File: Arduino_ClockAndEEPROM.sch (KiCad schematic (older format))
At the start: 13 parts, among them U1 24LC1025, U2 24LC1025, U3 DS1337_8pin_Bayterek, U4 ATmega328P-AU, Y1 Crystal, Y2 Crystal

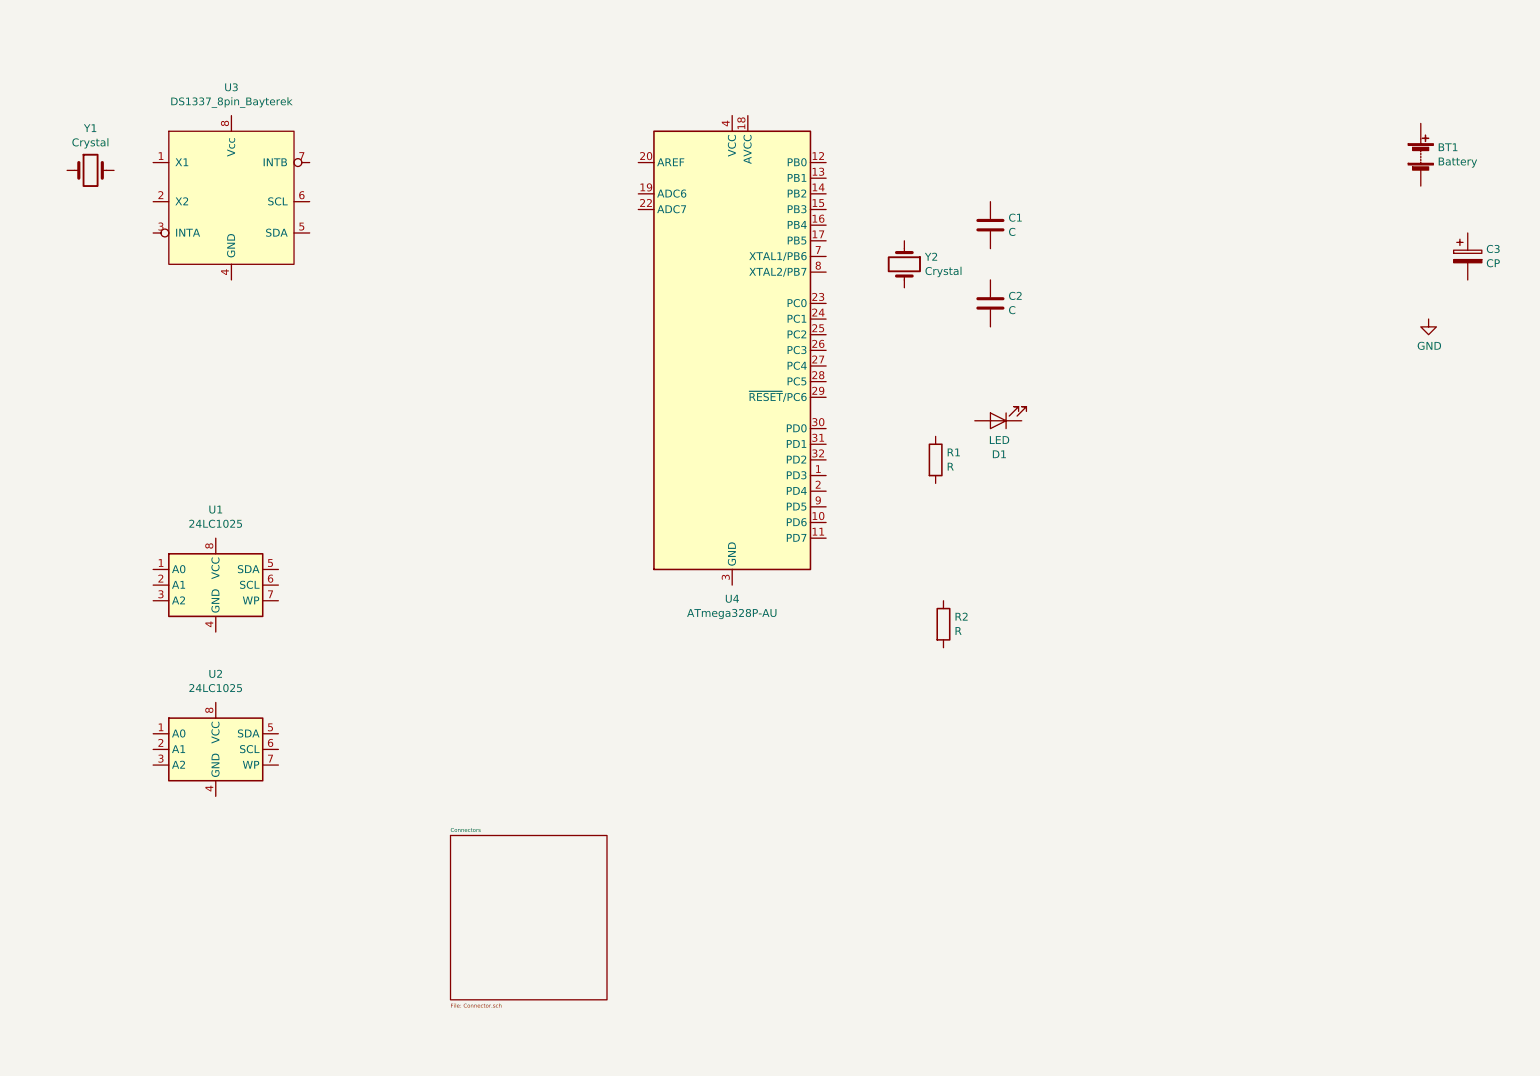
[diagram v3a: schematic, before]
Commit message: Completed associations and added component values.
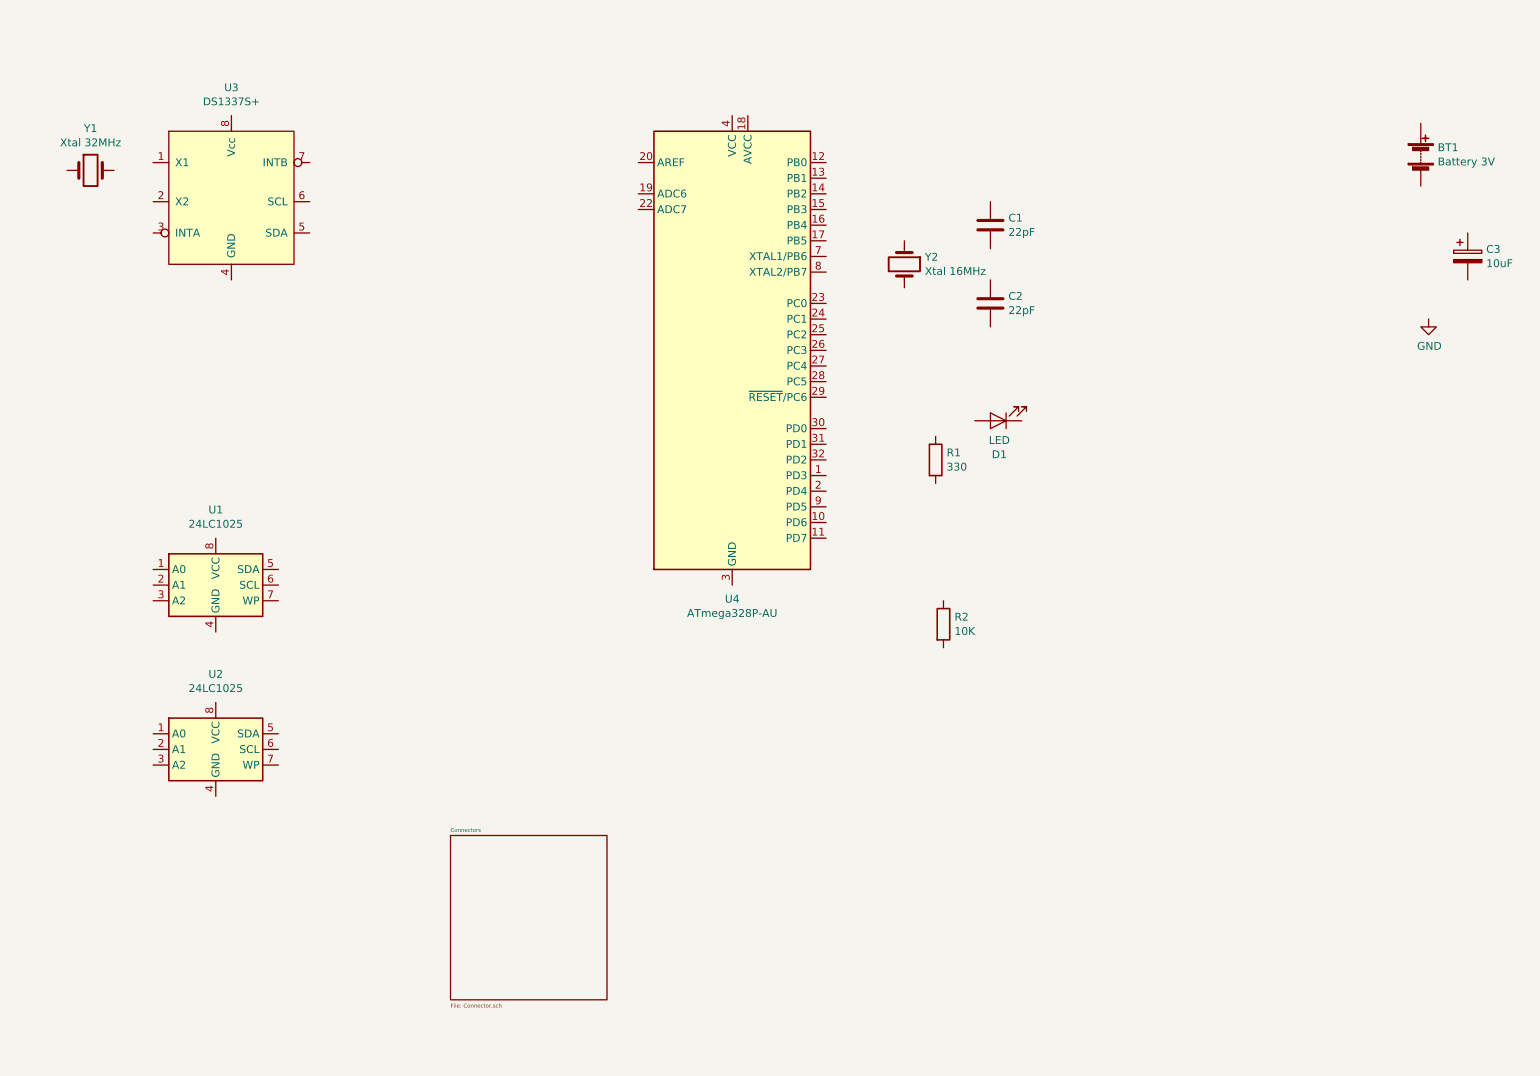
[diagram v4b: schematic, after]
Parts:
- BT1: value Battery -> Battery 3V; footprint (none) -> Connector_PinHeader_2.54mm:PinHeader_1x02_P2.54mm_Vertical
- C1, C2: value C -> 22pF; footprint (none) -> Capacitor_SMD:C_0805_2012Metric_Pad1.15x1.40mm_HandSolder
- C3: value CP -> 10uF; footprint (none) -> Capacitor_SMD:C_0805_2012Metric_Pad1.15x1.40mm_HandSolder
- D1: footprint (none) -> LED_SMD:LED_0805_2012Metric_Pad1.15x1.40mm_HandSolder
- R1: value R -> 330; footprint (none) -> Resistor_SMD:R_0815_2038Metric_Pad1.53x4.00mm_HandSolder
- R2: value R -> 10K; footprint (none) -> Resistor_SMD:R_0815_2038Metric_Pad1.53x4.00mm_HandSolder
- U1, U2: footprint (none) -> Package_SO:SOIJ-8_5.3x5.3mm_P1.27mm
- U3: value DS1337_8pin_Bayterek -> DS1337S+; footprint (none) -> Package_SO:SO-8_5.3x6.2mm_P1.27mm
- Y1: value Crystal -> Xtal 32MHz; footprint (none) -> Crystal:Crystal_SMD_MicroCrystal_CC7V-T1A-2Pin_3.2x1.5mm
- Y2: value Crystal -> Xtal 16MHz; footprint (none) -> Crystal:Crystal_SMD_5032-2Pin_5.0x3.2mm_HandSoldering
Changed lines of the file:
@@
 P 9750 1750
 F 0 "BT1" H 9858 1796 50  0000 L CNN
-F 1 "Battery" H 9858 1705 50  0000 L CNN
-F 2 "" V 9750 1810 50  0001 C CNN
+F 1 "Battery 3V" H 9858 1705 50  0000 L CNN
+F 2 "Connector_PinHeader_2.54mm:PinHeader_1x02_P2.54mm_Vertical" V 9750 1810 50  0001 C CNN
 F 3 "~" V 9750 1810 50  0001 C CNN
 	1    9750 1750
@@
 P 7000 2200
 F 0 "C1" H 7115 2246 50  0000 L CNN
-F 1 "C" H 7115 2155 50  0000 L CNN
-F 2 "" H 7038 2050 50  0001 C CNN
+F 1 "22pF" H 7115 2155 50  0000 L CNN
+F 2 "Capacitor_SMD:C_0805_2012Metric_Pad1.15x1.40mm_HandSolder" H 7038 2050 50  0001 C CNN
 F 3 "~" H 7000 2200 50  0001 C CNN
 	1    7000 2200
@@
 P 7000 2700
 F 0 "C2" H 7115 2746 50  0000 L CNN
-F 1 "C" H 7115 2655 50  0000 L CNN
-F 2 "" H 7038 2550 50  0001 C CNN
+F 1 "22pF" H 7115 2655 50  0000 L CNN
+F 2 "Capacitor_SMD:C_0805_2012Metric_Pad1.15x1.40mm_HandSolder" H 7038 2550 50  0001 C CNN
 F 3 "~" H 7000 2700 50  0001 C CNN
 	1    7000 2700
@@
 P 10050 2400
 F 0 "C3" H 10168 2446 50  0000 L CNN
-F 1 "CP" H 10168 2355 50  0000 L CNN
-F 2 "" H 10088 2250 50  0001 C CNN
+F 1 "10uF" H 10168 2355 50  0000 L CNN
+F 2 "Capacitor_SMD:C_0805_2012Metric_Pad1.15x1.40mm_HandSolder" H 10088 2250 50  0001 C CNN
 F 3 "~" H 10050 2400 50  0001 C CNN
 	1    10050 2400
@@
 F 0 "D1" H 7043 3666 50  0000 C CNN
 F 1 "LED" H 7043 3575 50  0000 C CNN
-F 2 "" H 7050 3450 50  0001 C CNN
+F 2 "LED_SMD:LED_0805_2012Metric_Pad1.15x1.40mm_HandSolder" H 7050 3450 50  0001 C CNN
 F 3 "~" H 7050 3450 50  0001 C CNN
 	1    7050 3450
@@
 P 6650 3700
 F 0 "R1" H 6720 3746 50  0000 L CNN
-F 1 "R" H 6720 3655 50  0000 L CNN
-F 2 "" V 6580 3700 50  0001 C CNN
+F 1 "330" H 6720 3655 50  0000 L CNN
+F 2 "Resistor_SMD:R_0815_2038Metric_Pad1.53x4.00mm_HandSolder" V 6580 3700 50  0001 C CNN
 F 3 "~" H 6650 3700 50  0001 C CNN
 	1    6650 3700
@@
 P 6700 4750
 F 0 "R2" H 6770 4796 50  0000 L CNN
-F 1 "R" H 6770 4705 50  0000 L CNN
-F 2 "" V 6630 4750 50  0001 C CNN
+F 1 "10K" H 6770 4705 50  0000 L CNN
+F 2 "Resistor_SMD:R_0815_2038Metric_Pad1.53x4.00mm_HandSolder" V 6630 4750 50  0001 C CNN
 F 3 "~" H 6700 4750 50  0001 C CNN
 	1    6700 4750
@@
 F 0 "U1" H 2050 4981 50  0000 C CNN
 F 1 "24LC1025" H 2050 4890 50  0000 C CNN
-F 2 "" H 2050 4500 50  0001 C CNN
+F 2 "Package_SO:SOIJ-8_5.3x5.3mm_P1.27mm" H 2050 4500 50  0001 C CNN
 F 3 "http://ww1.microchip.com/downloads/en/DeviceDoc/21941B.pdf" H 2050 4500 50  0001 C CNN
 	1    2050 4500
@@
 P 2750 1450
 F 0 "U3" H 2150 1579 49  0000 C CNN
-F 1 "DS1337_8pin_Bayterek" H 2150 1489 49  0000 C CNN
-F 2 "" H 2800 1550 49  0001 C CNN
+F 1 "DS1337S+" H 2150 1489 49  0000 C CNN
+F 2 "Package_SO:SO-8_5.3x6.2mm_P1.27mm" H 2800 1550 49  0001 C CNN
 F 3 "http://www.farnell.com/datasheets/2000844.pdf?_ga=2.2648176.1329014715.1559527073-834126407.1559527073" H 2800 1550 49  0001 C CNN
 	1    2750 1450
@@
 P 6450 2450
 F 0 "Y2" V 6404 2581 50  0000 L CNN
-F 1 "Crystal" V 6495 2581 50  0000 L CNN
-F 2 "" H 6450 2450 50  0001 C CNN
+F 1 "Xtal 16MHz" V 6495 2581 50  0000 L CNN
+F 2 "Crystal:Crystal_SMD_5032-2Pin_5.0x3.2mm_HandSoldering" H 6450 2450 50  0001 C CNN
 F 3 "~" H 6450 2450 50  0001 C CNN
 	1    6450 2450
@@
 P 1250 1850
 F 0 "Y1" H 1250 2118 50  0000 C CNN
-F 1 "Crystal" H 1250 2027 50  0000 C CNN
-F 2 "" H 1250 1850 50  0001 C CNN
+F 1 "Xtal 32MHz" H 1250 2027 50  0000 C CNN
+F 2 "Crystal:Crystal_SMD_MicroCrystal_CC7V-T1A-2Pin_3.2x1.5mm" H 1250 1850 50  0001 C CNN
 F 3 "~" H 1250 1850 50  0001 C CNN
 	1    1250 1850
@@
 F 0 "U2" H 2050 6031 50  0000 C CNN
 F 1 "24LC1025" H 2050 5940 50  0000 C CNN
-F 2 "" H 2050 5550 50  0001 C CNN
+F 2 "Package_SO:SOIJ-8_5.3x5.3mm_P1.27mm" H 2050 5550 50  0001 C CNN
 F 3 "http://ww1.microchip.com/downloads/en/DeviceDoc/21941B.pdf" H 2050 5550 50  0001 C CNN
 	1    2050 5550

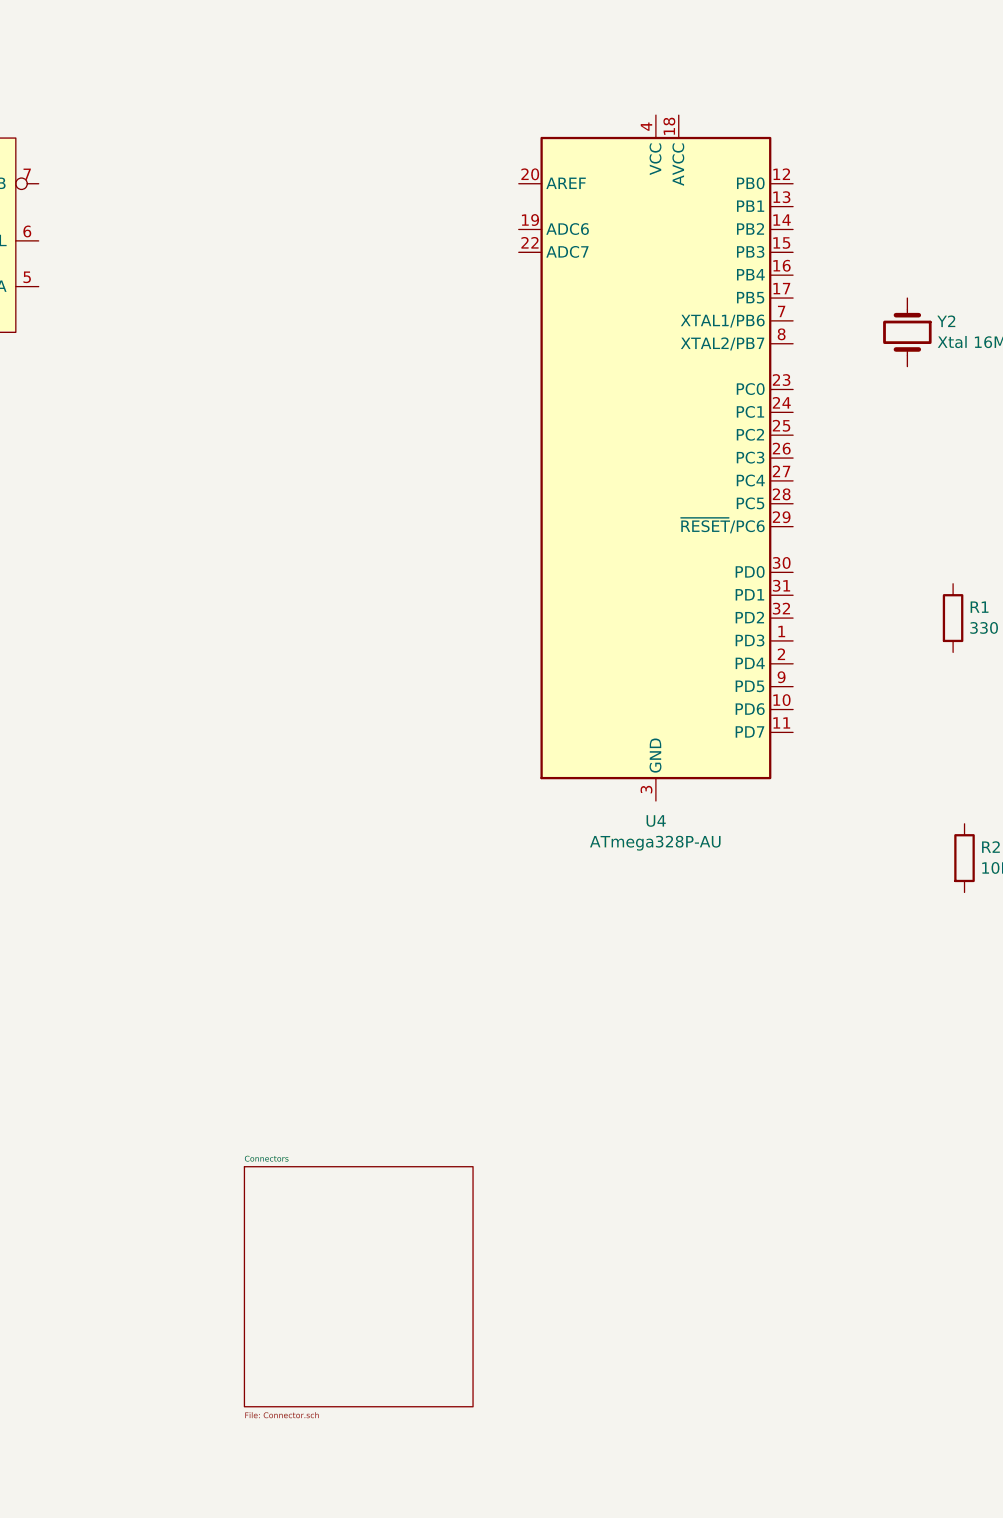
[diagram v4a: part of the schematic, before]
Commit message: Completed wiring in the connectors sheet.
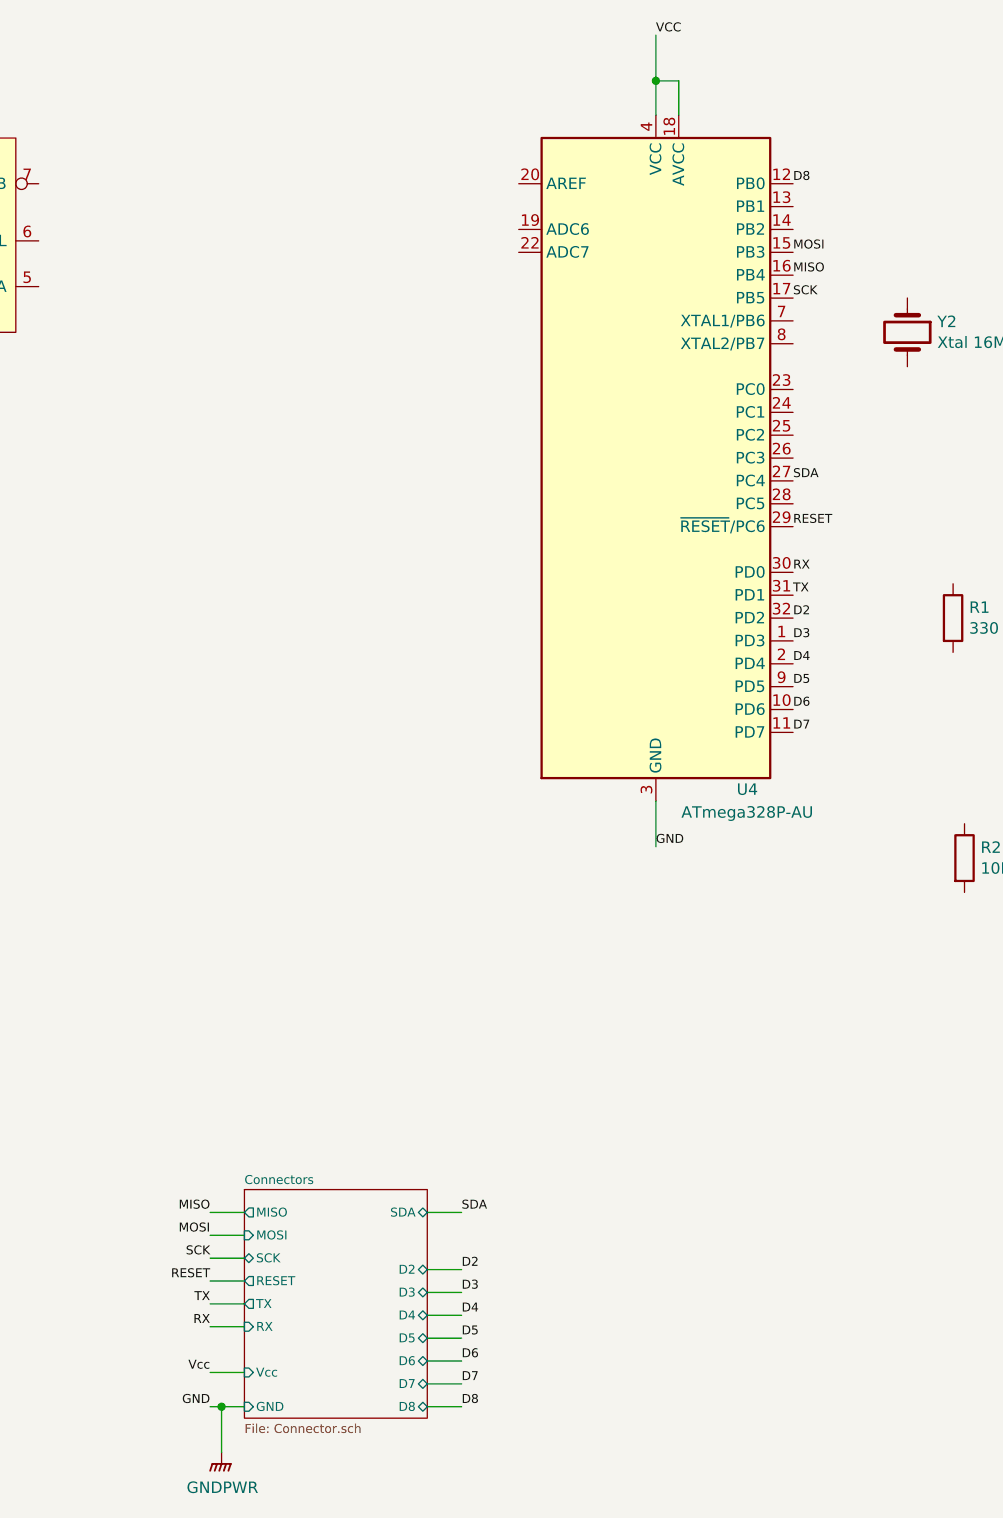
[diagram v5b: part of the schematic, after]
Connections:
- net GND: now also U4.21 (GND), U4.3 (GND), U4.5 (GND)
- net D3: now reaches U4.1 (PD3)
- net D6: now reaches U4.10 (PD6)
- net D7: now reaches U4.11 (PD7)
- net D8: now reaches U4.12 (PB0)
- net MOSI: now reaches U4.15 (PB3)
- net MISO: now reaches U4.16 (PB4)
- net SCK: now reaches U4.17 (PB5)
- net VCC: now reaches U4.18 (AVCC)
- net VCC: now also U4.4 (VCC), U4.6 (VCC)
- net D4: now reaches U4.2 (PD4)
- net SDA: now reaches U4.27 (PC4)
- net RESET: now reaches U4.29 (~RESET~/PC6)
- net RX: now reaches U4.30 (PD0)
- net TX: now reaches U4.31 (PD1)
- net D2: now reaches U4.32 (PD2)
- net D5: now reaches U4.9 (PD5)
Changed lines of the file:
@@
 U 1 1 5CF90E0E
 P 5350 3000
-F 0 "U4" H 5350 1411 50  0000 C CNN
-F 1 "ATmega328P-AU" H 5350 1320 50  0000 C CNN
+F 0 "U4" H 5750 1550 50  0000 C CNN
+F 1 "ATmega328P-AU" H 5750 1450 50  0000 C CNN
 F 2 "Package_QFP:TQFP-32_7x7mm_P0.8mm" H 5350 3000 50  0001 C CIN
 F 3 "http://ww1.microchip.com/downloads/en/DeviceDoc/ATmega328_P%20AVR%20MCU%20with%20picoPower%20Technology%20Data%20Sheet%2040001984A.pdf" H 5350 3000 50  0001 C CNN
@@
 	1    0    0    -1
 $EndComp
-$Sheet
-S 3550 6100 1000 1050
-U 5CF95995
-F0 "Connectors" 25
-F1 "Connector.sch" 25
-$EndSheet
 $Comp
 L Bayterek_Components:DS1337_8pin_Bayterek U3
@@
 	1    0    0    -1
 $EndComp
+Text Label 3400 6300 2    39   ~ 0
+MISO
+Wire Wire Line
+	3550 6300 3400 6300
+Text Label 5950 2200 0    39   ~ 0
+MISO
+Wire Wire Line
+	3550 6500 3400 6500
+Wire Wire Line
+	3550 6600 3400 6600
+Wire Wire Line
+	3550 7000 3400 7000
+Wire Wire Line
+	3550 6400 3400 6400
+Wire Wire Line
+	3550 7150 3450 7150
+Text Label 3400 6500 2    39   ~ 0
+SCK
+Text Label 3400 6600 2    39   ~ 0
+RESET
+Text Label 3400 7000 2    39   ~ 0
+Vcc
+Text Label 3400 6400 2    39   ~ 0
+MOSI
+Text Label 3400 7150 2    39   ~ 0
+GND
+Text Label 5950 2100 0    39   ~ 0
+MOSI
+Text Label 5950 2300 0    39   ~ 0
+SCK
+Text Label 5950 3300 0    39   ~ 0
+RESET
+Wire Wire Line
+	5350 1500 5350 1350
+Wire Wire Line
+	5350 1350 5450 1350
+Wire Wire Line
+	5450 1350 5450 1500
+Wire Wire Line
+	5350 1350 5350 1150
+Connection ~ 5350 1350
+Text Label 5350 1150 0    39   ~ 0
+VCC
+Wire Wire Line
+	5350 4500 5350 4700
+Text Label 5350 4700 0    39   ~ 0
+GND
+$Comp
+L power:GNDPWR #PWR?
+U 1 1 5CFC1B6B
+P 3450 7350
+F 0 "#PWR?" H 3450 7150 50  0001 C CNN
+F 1 "GNDPWR" H 3454 7196 50  0000 C CNN
+F 2 "" H 3450 7300 50  0001 C CNN
+F 3 "" H 3450 7300 50  0001 C CNN
+	1    3450 7350
+	1    0    0    -1
+$EndComp
+Wire Wire Line
+	3450 7350 3450 7150
+Connection ~ 3450 7150
+Wire Wire Line
+	3450 7150 3400 7150
+$Sheet
+S 3550 6200 800  1000
+U 5CF95995
+F0 "Connectors" 39
+F1 "Connector.sch" 39
+F2 "MISO" O L 3550 6300 39
+F3 "SCK" B L 3550 6500 39
+F4 "RESET" O L 3550 6600 39
+F5 "Vcc" I L 3550 7000 39
+F6 "MOSI" I L 3550 6400 39
+F7 "GND" I L 3550 7150 39
+F8 "RX" I L 3550 6800 39
+F9 "TX" O L 3550 6700 39
+F10 "SDA" B R 4350 6300 39
+F11 "D2" B R 4350 6550 39
+F12 "D3" B R 4350 6650 39
+F13 "D4" B R 4350 6750 39
+F14 "D5" B R 4350 6850 39
+F15 "D6" B R 4350 6950 39
+F16 "D7" B R 4350 7050 39
+F17 "D8" B R 4350 7150 39
+$EndSheet
+Wire Wire Line
+	3550 6800 3400 6800
+Wire Wire Line
+	3400 6700 3550 6700
+Wire Wire Line
+	4350 6300 4500 6300
+Wire Wire Line
+	4350 6550 4500 6550
+Wire Wire Line
+	4350 6650 4500 6650
+Wire Wire Line
+	4350 6750 4500 6750
+Wire Wire Line
+	4350 6850 4500 6850
+Wire Wire Line
+	4350 6950 4500 6950
+Wire Wire Line
+	4350 7050 4500 7050
+Wire Wire Line
+	4350 7150 4500 7150
+Text Label 3400 6800 2    39   ~ 0
+RX
+Text Label 3400 6700 2    39   ~ 0
+TX
+Text Label 4500 6300 0    39   ~ 0
+SDA
+Text Label 4500 6550 0    39   ~ 0
+D2
+Text Label 4500 6650 0    39   ~ 0
+D3
+Text Label 4500 6750 0    39   ~ 0
+D4
+Text Label 4500 6850 0    39   ~ 0
+D5
+Text Label 4500 6950 0    39   ~ 0
+D6
+Text Label 4500 7050 0    39   ~ 0
+D7
+Text Label 4500 7150 0    39   ~ 0
+D8
+Text Label 5950 3800 0    39   ~ 0
+D3
+Text Label 5950 3900 0    39   ~ 0
+D4
+Text Label 5950 4000 0    39   ~ 0
+D5
+Text Label 5950 4100 0    39   ~ 0
+D6
+Text Label 5950 4200 0    39   ~ 0
+D7
+Text Label 5950 1800 0    39   ~ 0
+D8
+Text Label 5950 3100 0    39   ~ 0
+SDA
+Text Label 5950 3500 0    39   ~ 0
+RX
+Text Label 5950 3600 0    39   ~ 0
+TX
+Text Label 5950 3700 0    39   ~ 0
+D2
 $EndSCHEMATC
